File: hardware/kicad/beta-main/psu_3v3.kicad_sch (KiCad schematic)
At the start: 0 parts

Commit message: tweaks and added servo controller
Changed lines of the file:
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@@
 		(comment 1 "Powers: DISPLAY")
+	)
+	(hierarchical_label "VIN"
+		(shape input)
+		(at 55.88 43.18 0)
+		(effects
+			(font
+				(size 1.27 1.27)
+			)
+			(justify left)
+		)
 	)
 	(hierarchical_label "3V3"

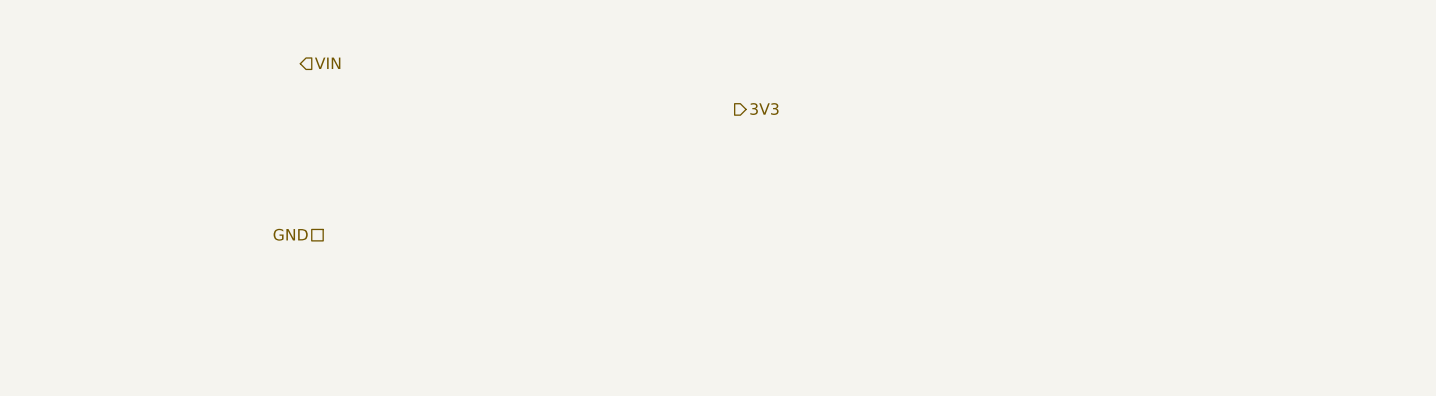
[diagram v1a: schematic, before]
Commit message: Dodanie schematu sekcji zasilania 3V3
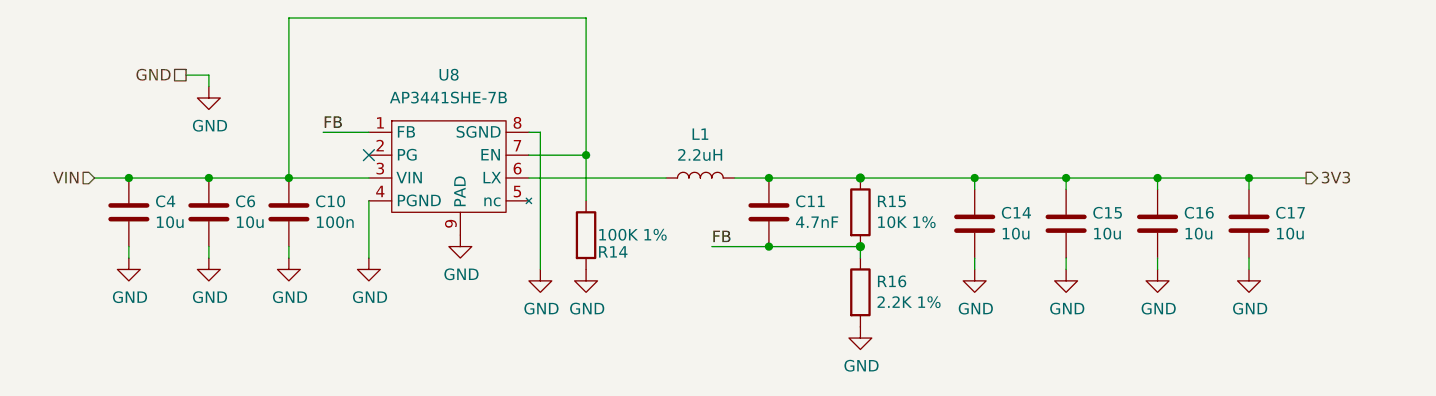
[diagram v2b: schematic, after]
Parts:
- added C10: 100n, Capacitor_SMD:C_0402_1005Metric, symbol Device:C
- added C11: 4.7nF, Capacitor_SMD:C_0402_1005Metric, symbol Device:C
- added C14, C15, C16, C17, C4, C6: 10u, Capacitor_SMD:C_0805_2012Metric, symbol Device:C
- added L1: 2.2uH, CM5IO:L_Bourns_SRP5030CC, symbol Device:L
- added R14: 100K 1%, Resistor_SMD:R_0402_1005Metric, symbol Device:R
- added R15: 10K 1%, Resistor_SMD:R_0402_1005Metric, symbol Device:R
- added R16: 2.2K 1%, Resistor_SMD:R_0402_1005Metric, symbol Device:R
- added U8: AP3441SHE-7B, Package_DFN_QFN:DFN-8-1EP_2x2mm_P0.5mm_EP1.05x1.75mm, symbol CM5IO:AP3441SHE-7B
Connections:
- net 3V3: now also C11.1, C14.1, C15.1, C16.1, C17.1, L1.2, R15.1
- net GND: now also C10.2, C14.2, C15.2, C16.2, C17.2, C4.2, C6.2, R14.2, R16.2, U8.4 (PGND), U8.8 (SGND), U8.9 (PAD)
- net VIN: now also C10.1, C4.1, C6.1, R14.1, U8.3 (VIN), U8.7 (EN)
- new net: L1.1, U8.6 (LX)
- new net FB: C11.2, R15.2, R16.1, U8.1 (FB)
- no-connect marks 0 -> 1

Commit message: 5V and amplifier corrections
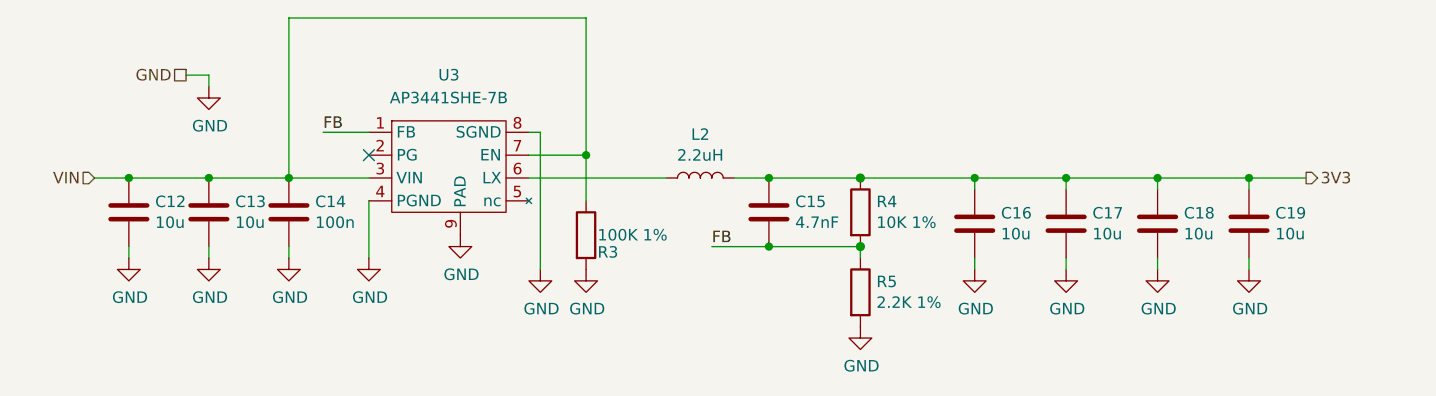
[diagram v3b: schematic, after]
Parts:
- renumbered C4 to C12, C6 to C13, C10 to C14, C11 to C15, C14 to C16, C15 to C17, C16 to C18, C17 to C19, L1 to L2, R14 to R3, R15 to R4, R16 to R5, U8 to U3

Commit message: Setup for PCB layout
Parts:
- C14: value 100n -> 0.1u
- L2: value 2.2uH -> 2.2u
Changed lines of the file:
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@@
 			)
 		)
-		(property "Value" "2.2uH"
+		(property "Value" "2.2u"
 			(at 100.33 53.3654 90)
 			(effects
@@
 			)
 		)
-		(property "Value" "100n"
+		(property "Value" "0.1u"
 			(at 57.531 60.833 0)
 			(effects

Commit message: remove power symbols from hierarchy and move different subsystems  around
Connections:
- net 3V3 renamed +3V3
- net VIN renamed +5V
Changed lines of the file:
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@@
+	)
+	(junction
+		(at 163.83 55.88)
+		(diameter 0)
+		(color 0 0 0 0)
 	)
 	(junction
@@
 	(wire
 		(pts
-			(xy 45.72 44.45) (xy 45.72 45.72)
-		)
-		(stroke
-			(width 0)
-			(type default)
-		)
-	)
-	(wire
-		(pts
 			(xy 104.14 55.88) (xy 107.95 55.88)
 		)
@@
 	(wire
 		(pts
-			(xy 161.29 55.88) (xy 167.64 55.88)
+			(xy 161.29 55.88) (xy 163.83 55.88)
 		)
 		(stroke
@@
 	(wire
 		(pts
+			(xy 36.83 63.5) (xy 36.83 64.77)
+		)
+		(stroke
+			(width 0)
+			(type default)
+		)
+	)
+	(wire
+		(pts
 			(xy 151.13 64.77) (xy 151.13 66.04)
 		)
@@
 	(wire
 		(pts
+			(xy 163.83 55.88) (xy 167.64 55.88)
+		)
+		(stroke
+			(width 0)
+			(type default)
+		)
+	)
+	(wire
+		(pts
 			(xy 54.61 63.5) (xy 54.61 64.77)
 		)
@@
 	(wire
 		(pts
-			(xy 43.18 44.45) (xy 45.72 44.45)
-		)
-		(stroke
-			(width 0)
-			(type default)
-		)
-	)
-	(wire
-		(pts
-			(xy 36.83 63.5) (xy 36.83 64.77)
-		)
-		(stroke
-			(width 0)
-			(type solid)
-		)
-	)
-	(wire
-		(pts
 			(xy 54.61 38.1) (xy 54.61 55.88)
 		)
@@
 		(pts
 			(xy 161.29 55.88) (xy 161.29 57.15)
+		)
+		(stroke
+			(width 0)
+			(type default)
+		)
+	)
+	(wire
+		(pts
+			(xy 163.83 52.07) (xy 163.83 55.88)
 		)
 		(stroke
@@
 			)
 			(justify left bottom)
-		)
-	)
-	(hierarchical_label "VIN"
-		(shape input)
-		(at 33.02 55.88 180)
-		(effects
-			(font
-				(size 1.27 1.27)
-			)
-			(justify right)
-		)
-	)
-	(hierarchical_label "3V3"
-		(shape output)
-		(at 167.64 55.88 0)
-		(effects
-			(font
-				(size 1.27 1.27)
-			)
-			(justify left)
-		)
-	)
-	(hierarchical_label "GND"
-		(shape passive)
-		(at 43.18 44.45 180)
-		(effects
-			(font
-				(size 1.27 1.27)
-			)
-			(justify right)
 		)
 	)
@@
 				(path "/ec75fd42-4efa-4f32-b57e-76d632cb46f5/a42372fe-a5e6-45a2-9241-7a7c7af267fd/261db230-bd2b-48a8-b49d-21eabae53d2d"
 					(reference "#PWR015")
+					(unit 1)
+				)
+			)
+		)
+	)
+	(symbol
+		(lib_id "power:PWR_FLAG")
+		(at 163.83 52.07 0)
+		(unit 1)
+		(exclude_from_sim no)
+		(in_bom yes)
+		(on_board yes)
+		(dnp no)
+		(fields_autoplaced yes)
+		(property "Reference" "#FLG03"
+			(at 163.83 50.165 0)
+			(effects
+				(font
+					(size 1.27 1.27)
+				)
+				(hide yes)
+			)
+		)
+		(property "Value" "PWR_FLAG"
+			(at 166.37 50.7999 0)
+			(effects
+				(font
+					(size 1.27 1.27)
+				)
+				(justify left)
+			)
+		)
+		(property "Footprint" ""
+			(at 163.83 52.07 0)
+			(effects
+				(font
+					(size 1.27 1.27)
+				)
+				(hide yes)
+			)
+		)
+		(property "Datasheet" "~"
+			(at 163.83 52.07 0)
+			(effects
+				(font
+					(size 1.27 1.27)
+				)
+				(hide yes)
+			)
+		)
+		(property "Description" "Special symbol for telling ERC where power comes from"
+			(at 163.83 52.07 0)
+			(effects
+				(font
+					(size 1.27 1.27)
+				)
+				(hide yes)
+			)
+		)
+		(pin "1"
+		)
+		(instances
+			(project "beta-main"
+				(path "/ec75fd42-4efa-4f32-b57e-76d632cb46f5/a42372fe-a5e6-45a2-9241-7a7c7af267fd/261db230-bd2b-48a8-b49d-21eabae53d2d"
+					(reference "#FLG03")
 					(unit 1)
 				)
@@
 	)
 	(symbol
+		(lib_id "power:+3V3")
+		(at 167.64 55.88 270)
+		(unit 1)
+		(exclude_from_sim no)
+		(in_bom yes)
+		(on_board yes)
+		(dnp no)
+		(fields_autoplaced yes)
+		(property "Reference" "#PWR04"
+			(at 163.83 55.88 0)
+			(effects
+				(font
+					(size 1.27 1.27)
+				)
+				(hide yes)
+			)
+		)
+		(property "Value" "+3V3"
+			(at 171.45 55.8799 90)
+			(effects
+				(font
+					(size 1.27 1.27)
+				)
+				(justify left)
+			)
+		)
+		(property "Footprint" ""
+			(at 167.64 55.88 0)
+			(effects
+				(font
+					(size 1.27 1.27)
+				)
+				(hide yes)
+			)
+		)
+		(property "Datasheet" ""
+			(at 167.64 55.88 0)
+			(effects
+				(font
+					(size 1.27 1.27)
+				)
+				(hide yes)
+			)
+		)
+		(property "Description" "Power symbol creates a global label with name \"+3V3\""
+			(at 167.64 55.88 0)
+			(effects
+				(font
+					(size 1.27 1.27)
+				)
+				(hide yes)
+			)
+		)
+		(pin "1"
+		)
+		(instances
+			(project ""
+				(path "/ec75fd42-4efa-4f32-b57e-76d632cb46f5/a42372fe-a5e6-45a2-9241-7a7c7af267fd/261db230-bd2b-48a8-b49d-21eabae53d2d"
+					(reference "#PWR04")
+					(unit 1)
+				)
+			)
+		)
+	)
+	(symbol
 		(lib_id "power:GND")
 		(at 82.55 66.04 0)
@@
 				(path "/ec75fd42-4efa-4f32-b57e-76d632cb46f5/a42372fe-a5e6-45a2-9241-7a7c7af267fd/261db230-bd2b-48a8-b49d-21eabae53d2d"
 					(reference "#PWR09")
-					(unit 1)
-				)
-			)
-		)
-	)
-	(symbol
-		(lib_id "power:GND")
-		(at 45.72 45.72 0)
-		(unit 1)
-		(exclude_from_sim no)
-		(in_bom yes)
-		(on_board yes)
-		(dnp no)
-		(property "Reference" "#PWR04"
-			(at 45.72 52.07 0)
-			(effects
-				(font
-					(size 1.27 1.27)
-				)
-				(hide yes)
-			)
-		)
-		(property "Value" "GND"
-			(at 45.847 50.1142 0)
-			(effects
-				(font
-					(size 1.27 1.27)
-				)
-			)
-		)
-		(property "Footprint" ""
-			(at 45.72 45.72 0)
-			(effects
-				(font
-					(size 1.27 1.27)
-				)
-				(hide yes)
-			)
-		)
-		(property "Datasheet" ""
-			(at 45.72 45.72 0)
-			(effects
-				(font
-					(size 1.27 1.27)
-				)
-				(hide yes)
-			)
-		)
-		(property "Description" "Power symbol creates a global label with name \"GND\" , ground"
-			(at 45.72 45.72 0)
-			(effects
-				(font
-					(size 1.27 1.27)
-				)
-				(hide yes)
-			)
-		)
-		(pin "1"
-		)
-		(instances
-			(project "psu_3v3"
-				(path "/51eb0c50-8d64-40b4-9f41-bc6e5bfb9a3a"
-					(reference "#PWR01")
-					(unit 1)
-				)
-			)
-			(project "beta-main"
-				(path "/ec75fd42-4efa-4f32-b57e-76d632cb46f5/a42372fe-a5e6-45a2-9241-7a7c7af267fd/261db230-bd2b-48a8-b49d-21eabae53d2d"
-					(reference "#PWR04")
 					(unit 1)
 				)
@@
 					(unit 1)
 				)
+			)
+		)
+	)
+	(symbol
+		(lib_id "power:+5V")
+		(at 33.02 55.88 90)
+		(unit 1)
+		(exclude_from_sim no)
+		(in_bom yes)
+		(on_board yes)
+		(dnp no)
+		(fields_autoplaced yes)
+		(property "Reference" "#PWR0112"
+			(at 36.83 55.88 0)
+			(effects
+				(font
+					(size 1.27 1.27)
+				)
+				(hide yes)
+			)
+		)
+		(property "Value" "+5V"
+			(at 29.21 55.8799 90)
+			(effects
+				(font
+					(size 1.27 1.27)
+				)
+				(justify left)
+			)
+		)
+		(property "Footprint" ""
+			(at 33.02 55.88 0)
+			(effects
+				(font
+					(size 1.27 1.27)
+				)
+				(hide yes)
+			)
+		)
+		(property "Datasheet" ""
+			(at 33.02 55.88 0)
+			(effects
+				(font
+					(size 1.27 1.27)
+				)
+				(hide yes)
+			)
+		)
+		(property "Description" "Power symbol creates a global label with name \"+5V\""
+			(at 33.02 55.88 0)
+			(effects
+				(font
+					(size 1.27 1.27)
+				)
+				(hide yes)
+			)
+		)
+		(pin "1"
+		)
+		(instances
+			(project ""
+				(path "/ec75fd42-4efa-4f32-b57e-76d632cb46f5/a42372fe-a5e6-45a2-9241-7a7c7af267fd/261db230-bd2b-48a8-b49d-21eabae53d2d"
+					(reference "#PWR0112")
+					(unit 1)
+				)

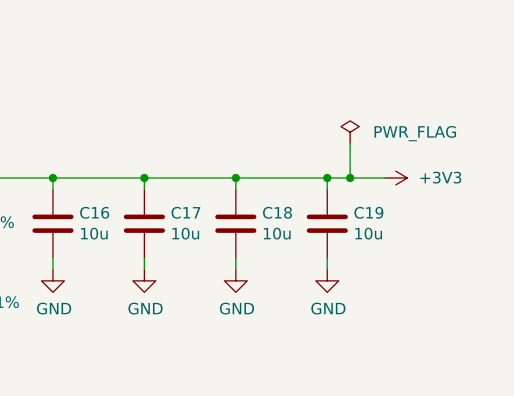
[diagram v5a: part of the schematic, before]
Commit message: Rough layout with all elements, test point for 3V3 added. C footprints need to change to 6 3
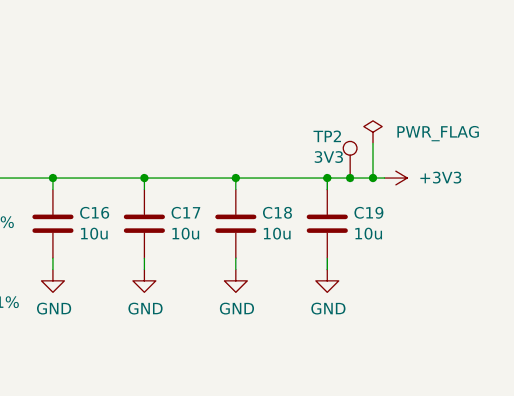
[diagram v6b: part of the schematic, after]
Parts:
- added TP2: 3V3, TestPoint:TestPoint_Pad_D1.0mm, symbol Connector:TestPoint
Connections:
- net +3V3: now also TP2.1
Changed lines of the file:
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@@
+	)
+	(junction
+		(at 166.37 55.88)
+		(diameter 0)
+		(color 0 0 0 0)
 	)
 	(junction
@@
 	)
 	(junction
-		(at 163.83 55.88)
-		(diameter 0)
-		(color 0 0 0 0)
-	)
-	(junction
 		(at 151.13 55.88)
 		(diameter 0)
@@
 		(color 0 0 0 0)
 	)
+	(junction
+		(at 163.83 55.88)
+		(diameter 0)
+		(color 0 0 0 0)
+	)
 	(no_connect
 		(at 63.5 53.34)
@@
 	(wire
 		(pts
+			(xy 163.83 55.88) (xy 166.37 55.88)
+		)
+		(stroke
+			(width 0)
+			(type default)
+		)
+	)
+	(wire
+		(pts
 			(xy 33.02 55.88) (xy 36.83 55.88)
 		)
@@
 	(wire
 		(pts
-			(xy 163.83 55.88) (xy 167.64 55.88)
+			(xy 166.37 55.88) (xy 167.64 55.88)
 		)
 		(stroke
@@
 	(wire
 		(pts
-			(xy 163.83 52.07) (xy 163.83 55.88)
+			(xy 166.37 52.07) (xy 166.37 55.88)
 		)
 		(stroke
@@
 	(symbol
 		(lib_id "power:PWR_FLAG")
-		(at 163.83 52.07 0)
+		(at 166.37 52.07 0)
 		(unit 1)
 		(exclude_from_sim no)
@@
 		(fields_autoplaced yes)
 		(property "Reference" "#FLG03"
-			(at 163.83 50.165 0)
+			(at 166.37 50.165 0)
 			(effects
 				(font
@@
 		)
 		(property "Value" "PWR_FLAG"
-			(at 166.37 50.7999 0)
+			(at 168.91 50.7999 0)
 			(effects
 				(font
@@
 		)
 		(property "Footprint" ""
-			(at 163.83 52.07 0)
+			(at 166.37 52.07 0)
 			(effects
 				(font
@@
 		)
 		(property "Datasheet" "~"
-			(at 163.83 52.07 0)
+			(at 166.37 52.07 0)
 			(effects
 				(font
@@
 		)
 		(property "Description" "Special symbol for telling ERC where power comes from"
-			(at 163.83 52.07 0)
+			(at 166.37 52.07 0)
 			(effects
 				(font
@@
 					(unit 1)
 				)
+			)
+		)
+	)
+	(symbol
+		(lib_id "Connector:TestPoint")
+		(at 163.83 55.88 0)
+		(unit 1)
+		(exclude_from_sim no)
+		(in_bom yes)
+		(on_board yes)
+		(dnp no)
+		(property "Reference" "TP2"
+			(at 159.766 51.308 0)
+			(effects
+				(font
+					(size 1.27 1.27)
+				)
+				(justify left)
+			)
+		)
+		(property "Value" "3V3"
+			(at 159.766 53.594 0)
+			(effects
+				(font
+					(size 1.27 1.27)
+				)
+				(justify left)
+			)
+		)
+		(property "Footprint" "TestPoint:TestPoint_Pad_D1.0mm"
+			(at 168.91 55.88 0)
+			(effects
+				(font
+					(size 1.27 1.27)
+				)
+				(hide yes)
+			)
+		)
+		(property "Datasheet" "~"
+			(at 168.91 55.88 0)
+			(effects
+				(font
+					(size 1.27 1.27)
+				)
+				(hide yes)
+			)
+		)
+		(property "Description" "test point"
+			(at 163.83 55.88 0)
+			(effects
+				(font
+					(size 1.27 1.27)
+				)
+				(hide yes)
+			)
+		)
+		(pin "1"
+		)
+		(instances
+			(project "beta-main"
+				(path "/ec75fd42-4efa-4f32-b57e-76d632cb46f5/a42372fe-a5e6-45a2-9241-7a7c7af267fd/261db230-bd2b-48a8-b49d-21eabae53d2d"
+					(reference "TP2")
+					(unit 1)
+				)

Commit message: Footprints changed to 603
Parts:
- C12, C13, C16, C17, C18, C19: footprint Capacitor_SMD:C_0805_2012Metric -> Capacitor_SMD:C_0603_1608Metric_Pad1.08x0.95mm_HandSolder
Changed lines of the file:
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@@
 			)
 		)
-		(property "Footprint" "Capacitor_SMD:C_0805_2012Metric"
+		(property "Footprint" "Capacitor_SMD:C_0603_1608Metric_Pad1.08x0.95mm_HandSolder"
 			(at 152.0952 64.77 0)
 			(effects
@@
 			)
 		)
-		(property "Footprint" "Capacitor_SMD:C_0805_2012Metric"
+		(property "Footprint" "Capacitor_SMD:C_0603_1608Metric_Pad1.08x0.95mm_HandSolder"
 			(at 46.6852 63.5 0)
 			(effects
@@
 			)
 		)
-		(property "Footprint" "Capacitor_SMD:C_0805_2012Metric"
+		(property "Footprint" "Capacitor_SMD:C_0603_1608Metric_Pad1.08x0.95mm_HandSolder"
 			(at 37.7952 63.5 0)
 			(effects
@@
 			)
 		)
-		(property "Footprint" "Capacitor_SMD:C_0805_2012Metric"
+		(property "Footprint" "Capacitor_SMD:C_0603_1608Metric_Pad1.08x0.95mm_HandSolder"
 			(at 131.7752 64.77 0)
 			(effects
@@
 			)
 		)
-		(property "Footprint" "Capacitor_SMD:C_0805_2012Metric"
+		(property "Footprint" "Capacitor_SMD:C_0603_1608Metric_Pad1.08x0.95mm_HandSolder"
 			(at 141.9352 64.77 0)
 			(effects
@@
 			)
 		)
-		(property "Footprint" "Capacitor_SMD:C_0805_2012Metric"
+		(property "Footprint" "Capacitor_SMD:C_0603_1608Metric_Pad1.08x0.95mm_HandSolder"
 			(at 162.2552 64.77 0)
 			(effects
